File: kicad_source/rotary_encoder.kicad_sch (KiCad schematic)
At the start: 4 parts, among them SW2 RotaryEncoder_Switch_MP

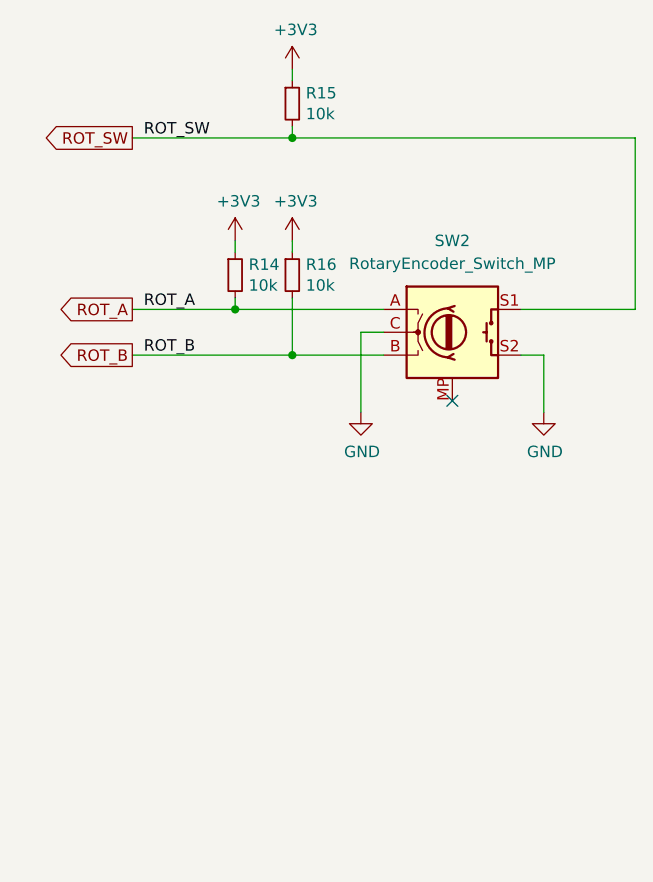
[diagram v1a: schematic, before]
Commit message: added push button
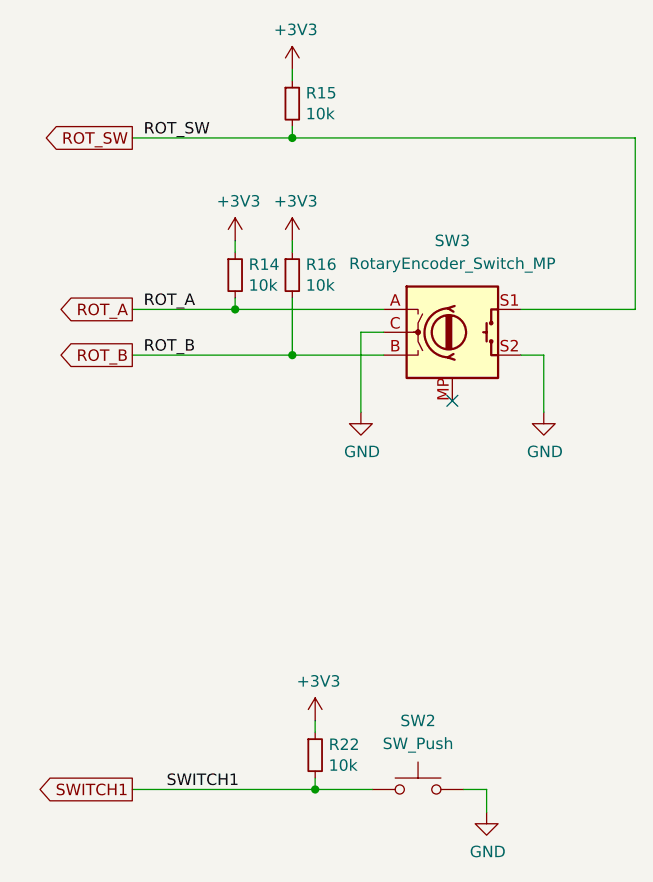
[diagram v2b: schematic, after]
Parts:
- added R22: 10k, Resistor_SMD:R_0603_1608Metric, symbol Device:R_Small
- added SW2: SW_Push, Button_Switch_SMD:SW_SPST_Omron_B3FS-100xP, symbol Switch:SW_Push
- renumbered SW2 to SW3
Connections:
- net +3V3: now also R22.1
- net GND: now also SW2.2
- new net SWITCH1: R22.2, SW2.1
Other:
- title: CyphalIMUBase/CAN -> CyphalHMIBase/CAN
